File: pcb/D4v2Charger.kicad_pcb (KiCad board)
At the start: 2 copper layers, 21.6 x 20.6 mm, 16 parts, among them J1 Conn_01x02_Pin, U1 BQ25185DLHR

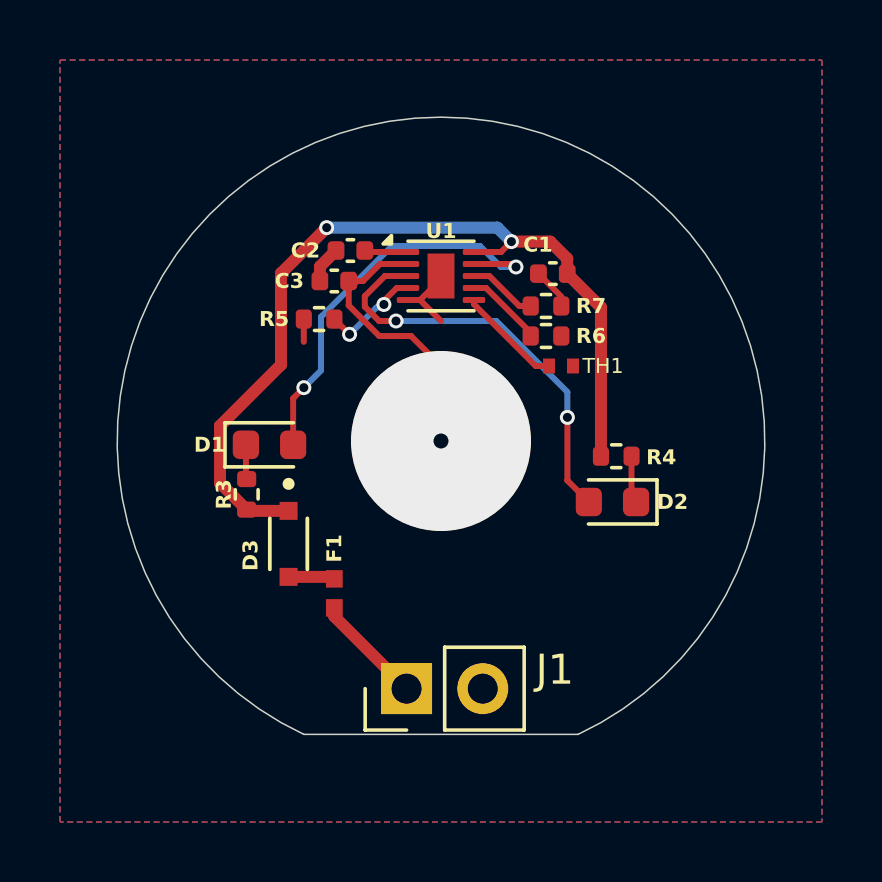
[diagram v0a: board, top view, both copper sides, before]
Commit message: add gnd stitch vias
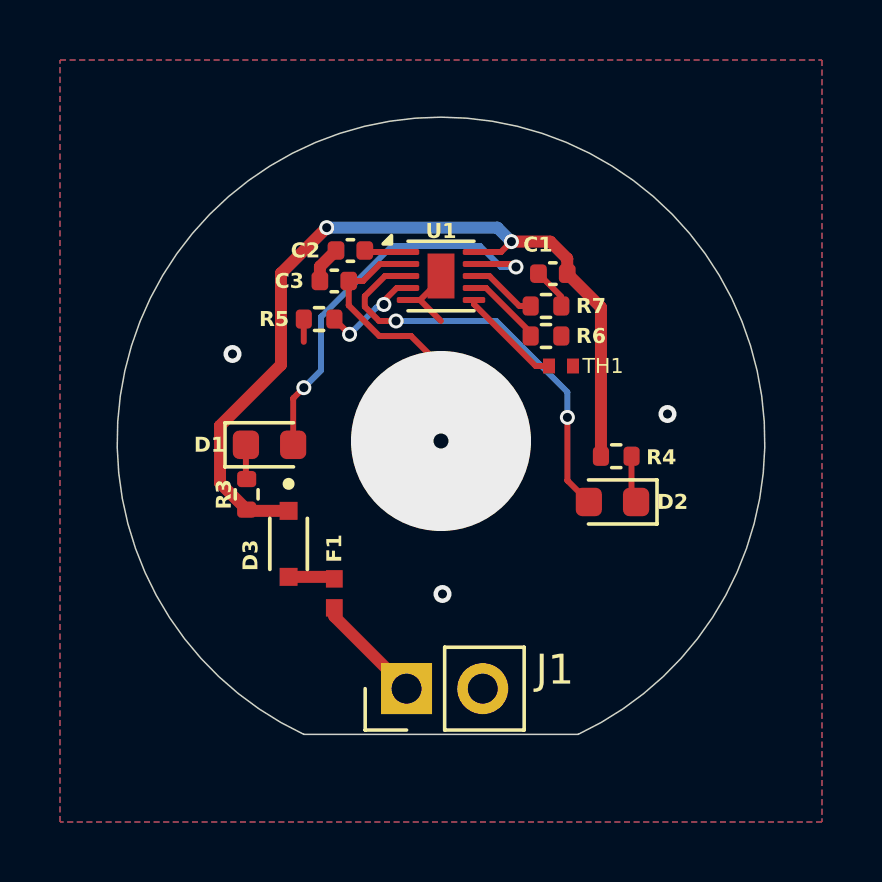
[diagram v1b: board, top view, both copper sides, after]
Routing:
- net GND: vias 0 -> 3
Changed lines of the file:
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@@
+		(net 1)
+	)
+	(via
+		(at 171.5 94)
+		(size 0.6)
+		(drill 0.3)
+		(layers "F.Cu" "B.Cu")
+		(free yes)
+		(net 1)
+	)
+	(via
+		(at 164.5 86)
+		(size 0.6)
+		(drill 0.3)
+		(layers "F.Cu" "B.Cu")
+		(free yes)
+		(net 1)
+	)
+	(via
+		(at 179 88)
+		(size 0.6)
+		(drill 0.3)
+		(layers "F.Cu" "B.Cu")
+		(free yes)
 		(net 1)
 	)

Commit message: update edge cuts
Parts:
- moved J1 0.13 mm to (170.3, 97.0)
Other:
- board size 21.6 x 20.6 mm -> 20.5 x 19.8 mm
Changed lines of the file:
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@@
 	(footprint "Connector_PinHeader_2.54mm:PinHeader_1x02_P2.54mm_Vertical"
 		(layer "F.Cu")
-		(at 170.302 97.155 90)
+		(at 170.302 97.028 90)
 		(descr "Through hole straight pin header, 1x02, 2.54mm pitch, single row")
 		(tags "Through hole pin header THT 1x02 2.54mm single row")
@@
 	)
 	(gr_arc
-		(start 166.878 98.679)
-		(mid 171.45 78.105)
-		(end 176.022 98.679)
+		(start 167.64 98.425)
+		(mid 171.45 78.641261)
+		(end 175.26 98.425)
 		(stroke
-			(width 4)
+			(width 2)
 			(type solid)
 		)
@@
 	)
 	(gr_arc
-		(start 166.878 98.679)
-		(mid 171.45 78.105)
-		(end 176.022 98.679)
+		(start 167.64 98.424998)
+		(mid 171.45 78.641259)
+		(end 175.26 98.424998)
 		(stroke
-			(width 4)
+			(width 2)
 			(type solid)
 		)
@@
 	)
 	(gr_arc
-		(start 166.878 98.679)
-		(mid 171.45 78.105)
-		(end 176.022 98.679)
+		(start 167.64 98.425)
+		(mid 171.45 78.641261)
+		(end 175.26 98.425)
 		(stroke
 			(width 0.05)
@@
 	)
 	(gr_line
-		(start 176.022 98.679)
-		(end 166.878 98.679)
+		(start 175.26 98.424998)
+		(end 167.640001 98.425)
 		(stroke
 			(width 0.05)
@@
 	)
 	(segment
+		(start 167.894 94.62)
+		(end 170.302 97.028)
+		(width 0.4)
+		(layer "F.Cu")
+		(net 14)
+	)
+	(segment
 		(start 167.894 94.463)
-		(end 167.894 94.747)
-		(width 0.4)
-		(layer "F.Cu")
-		(net 14)
-	)
-	(segment
-		(start 167.894 94.747)
-		(end 170.302 97.155)
-		(width 0.4)
-		(layer "F.Cu")
+		(end 167.894 94.62)
+		(width 0.4)
+		(layer "F.Cu")
